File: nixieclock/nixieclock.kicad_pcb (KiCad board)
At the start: 2 copper layers, 21 parts, among them Q1 IRLR3110ZTRPBF, U1 LT3757AEMSE

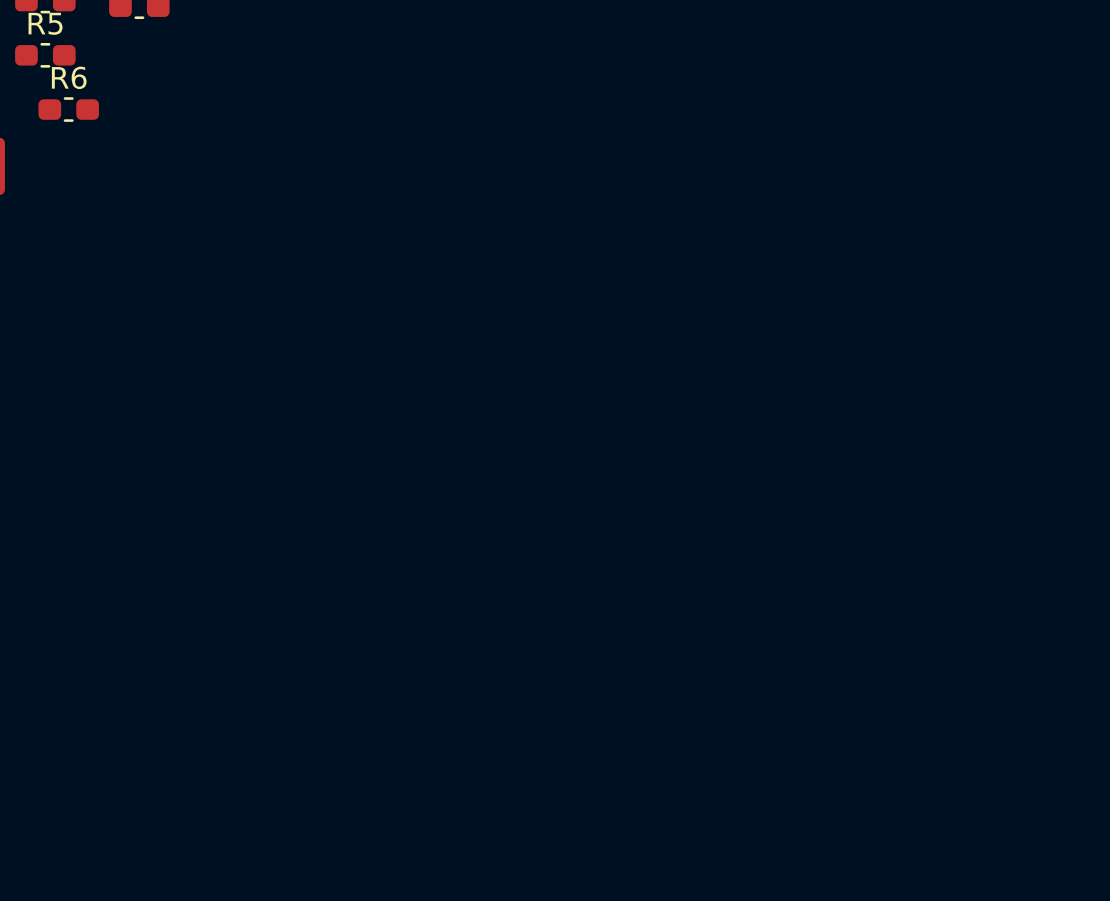
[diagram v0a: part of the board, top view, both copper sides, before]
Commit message: added nixie breakout, began shift registers
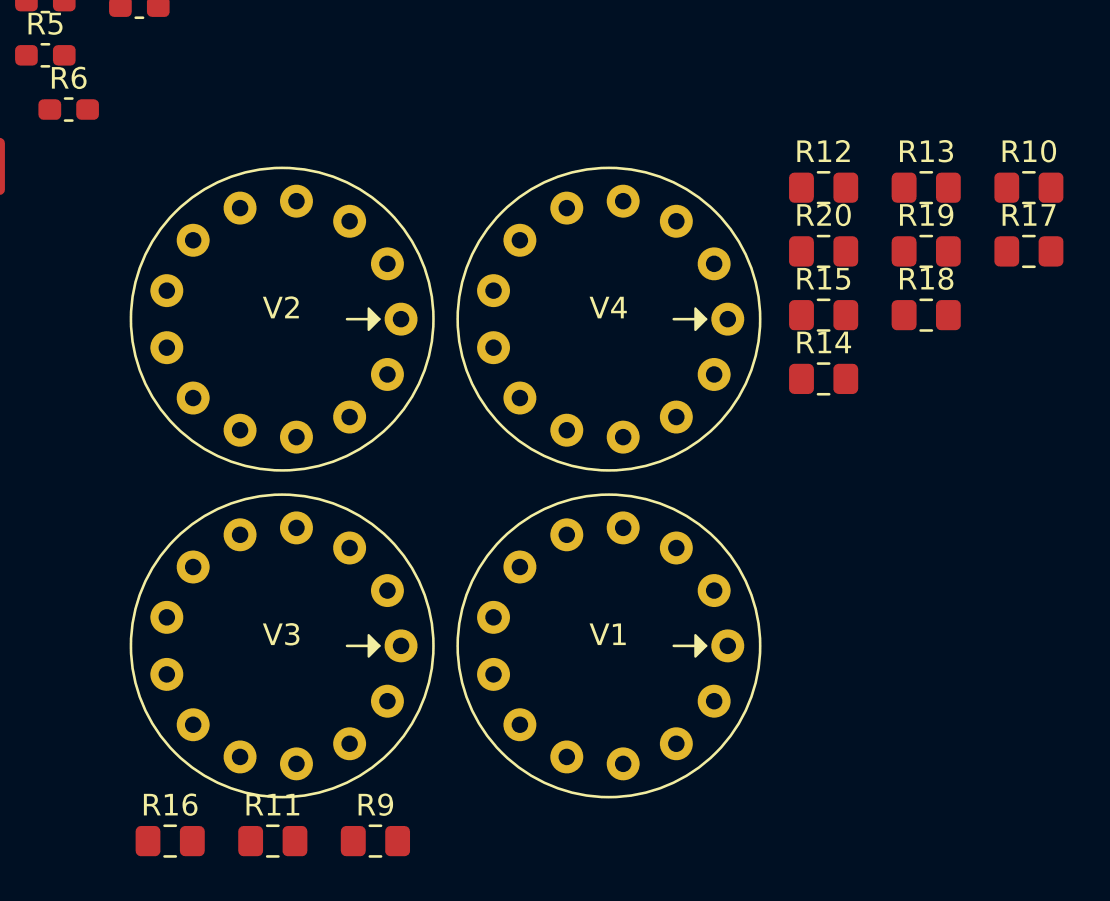
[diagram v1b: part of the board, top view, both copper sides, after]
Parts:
- added R10: R, Resistor_SMD:R_0805_2012Metric_Pad1.15x1.40mm_HandSolder, F.Cu at (261.4, 82.8)
- added R11: R, Resistor_SMD:R_0805_2012Metric_Pad1.15x1.40mm_HandSolder, F.Cu at (226.4, 113.0)
- added R12: R, Resistor_SMD:R_0805_2012Metric_Pad1.15x1.40mm_HandSolder, F.Cu at (251.9, 82.8)
- added R13: R, Resistor_SMD:R_0805_2012Metric_Pad1.15x1.40mm_HandSolder, F.Cu at (256.7, 82.8)
- added R14: R, Resistor_SMD:R_0805_2012Metric_Pad1.15x1.40mm_HandSolder, F.Cu at (251.9, 91.6)
- added R15: R, Resistor_SMD:R_0805_2012Metric_Pad1.15x1.40mm_HandSolder, F.Cu at (251.9, 88.7)
- added R16: R, Resistor_SMD:R_0805_2012Metric_Pad1.15x1.40mm_HandSolder, F.Cu at (221.7, 113.0)
- added R17: R, Resistor_SMD:R_0805_2012Metric_Pad1.15x1.40mm_HandSolder, F.Cu at (261.4, 85.7)
- added R18: R, Resistor_SMD:R_0805_2012Metric_Pad1.15x1.40mm_HandSolder, F.Cu at (256.7, 88.7)
- added R19: R, Resistor_SMD:R_0805_2012Metric_Pad1.15x1.40mm_HandSolder, F.Cu at (256.7, 85.7)
- added R20: R, Resistor_SMD:R_0805_2012Metric_Pad1.15x1.40mm_HandSolder, F.Cu at (251.9, 85.7)
- added R9: R, Resistor_SMD:R_0805_2012Metric_Pad1.15x1.40mm_HandSolder, F.Cu at (231.2, 113.0)
- added V1: IN14, Personal:IN-14, F.Cu at (242.0, 104.0)
- added V2: IN14, Personal:IN-14, F.Cu at (226.9, 88.9)
- added V3: IN14, Personal:IN-14, F.Cu at (226.9, 104.0)
- added V4: IN14, Personal:IN-14, F.Cu at (242.0, 88.9)

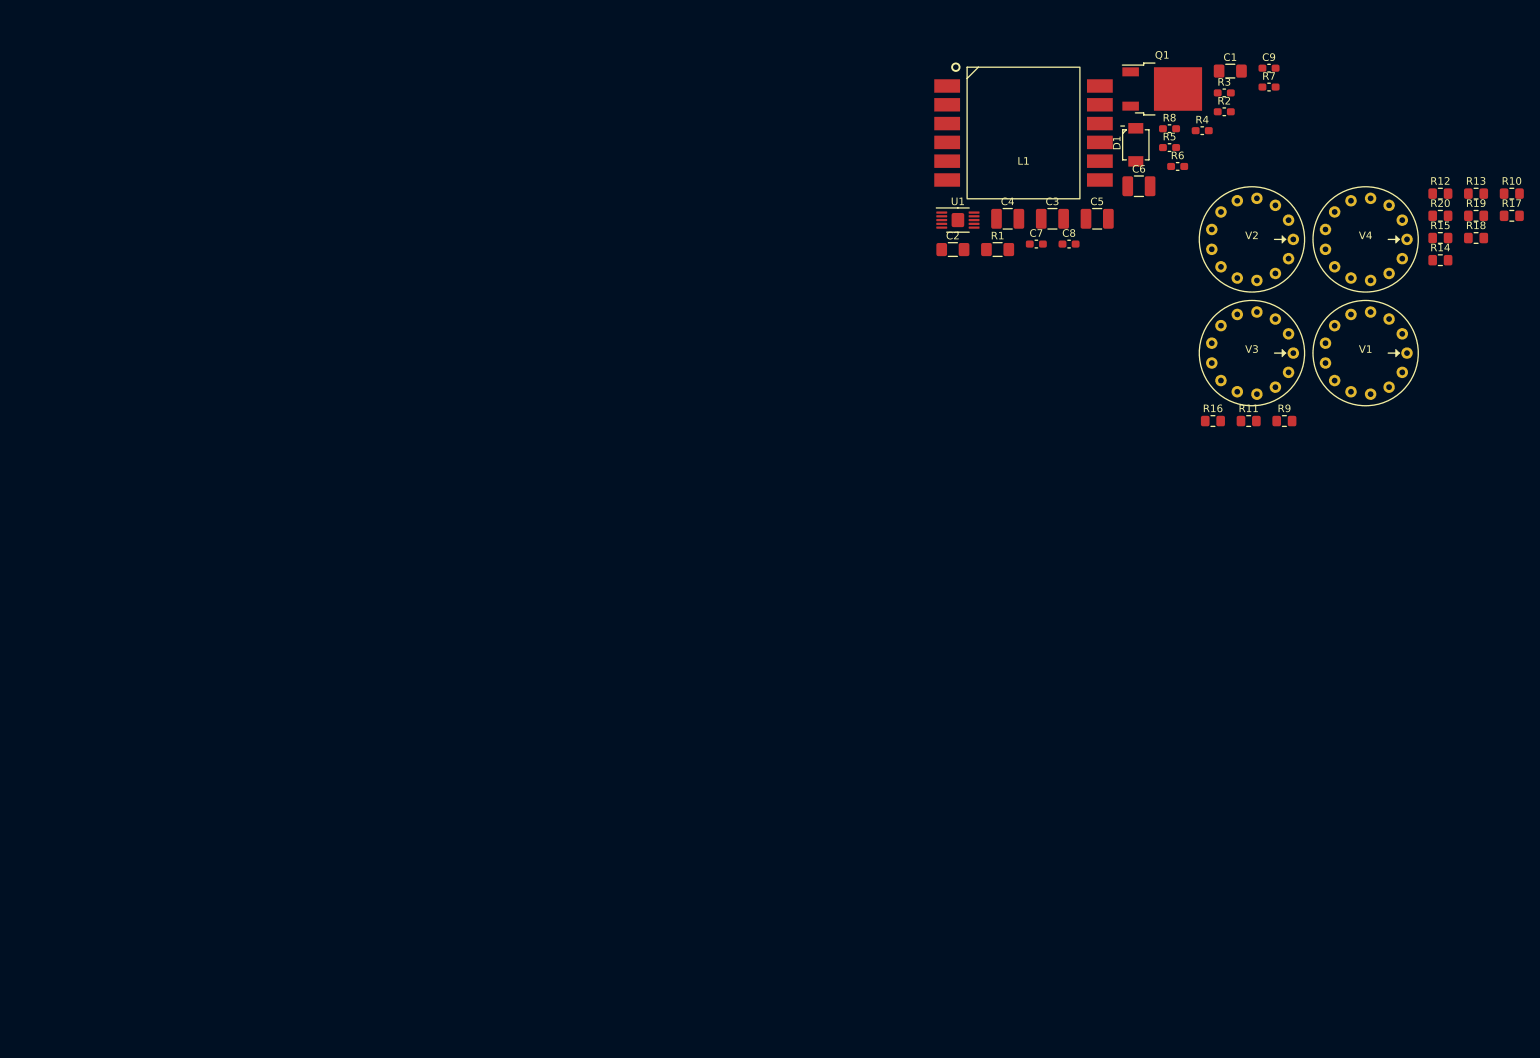
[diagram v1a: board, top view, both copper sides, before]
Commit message: finalized power supplies, most footprints, nixie breakout
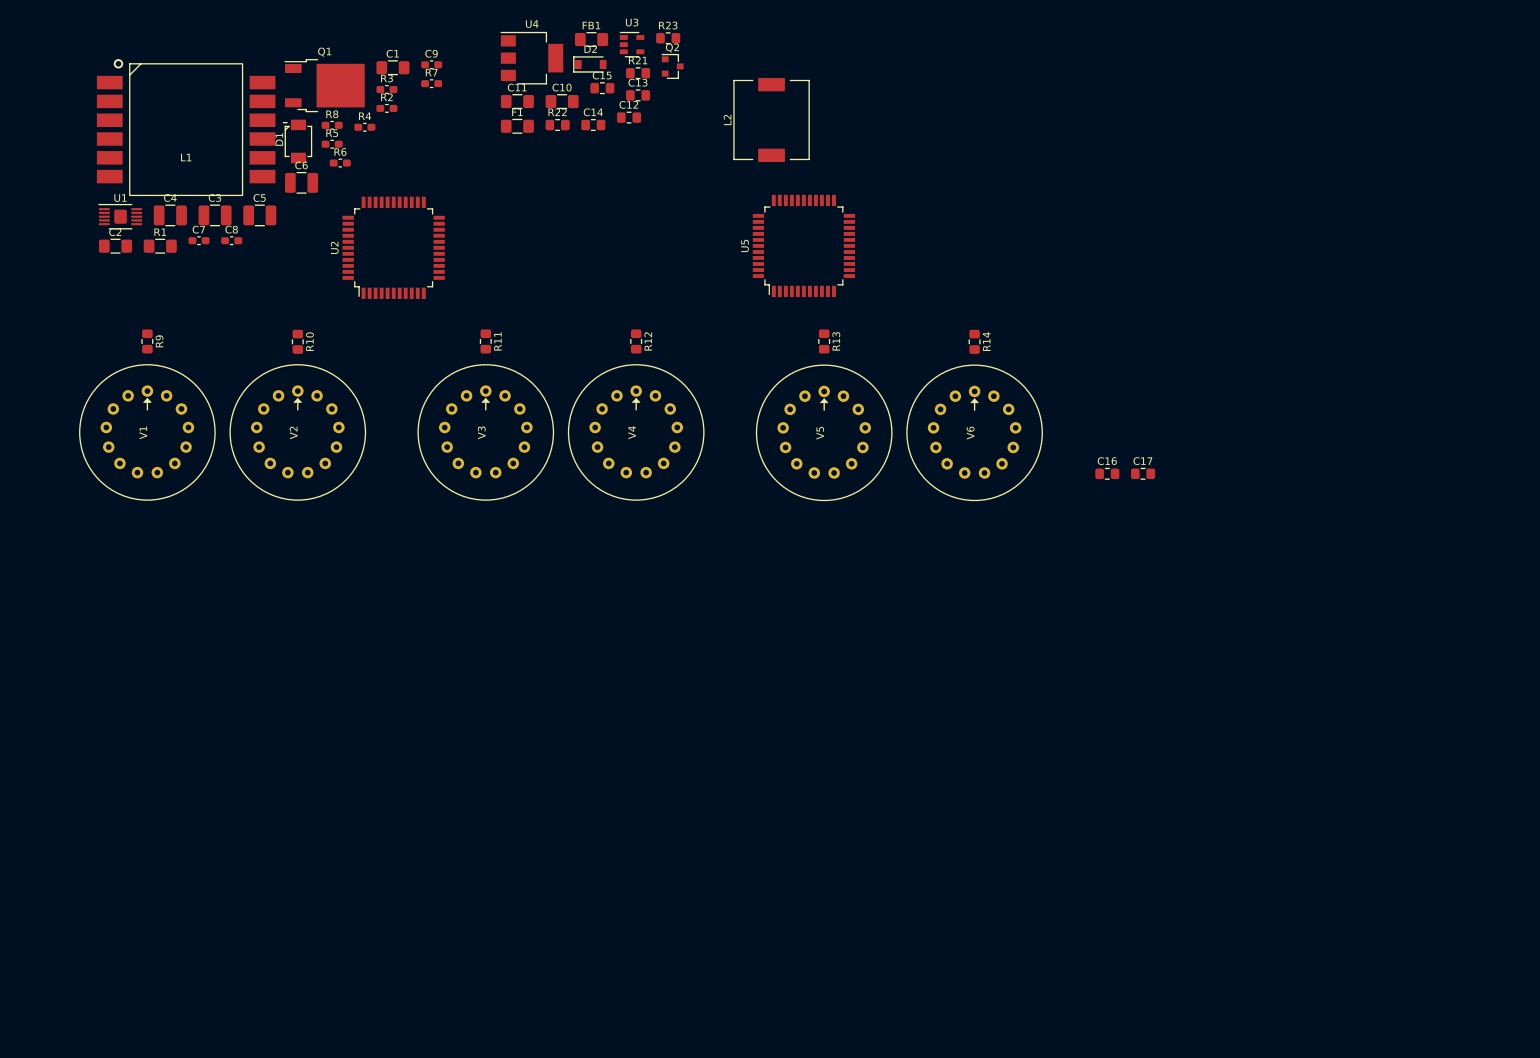
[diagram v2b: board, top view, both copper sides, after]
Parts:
- removed R15, R16, R17, R18, R19, R20: R, Resistor_SMD:R_0805_2012Metric_Pad1.15x1.40mm_HandSolder
- added C10: 10uF, Capacitor_SMD:C_1206_3216Metric_Pad1.42x1.75mm_HandSolder, F.Cu at (135.2, 70.5)
- added C11: 4.7uF, Capacitor_SMD:C_1206_3216Metric_Pad1.42x1.75mm_HandSolder, F.Cu at (129.2, 70.5)
- added C12: 2.2uF, Capacitor_SMD:C_0805_2012Metric_Pad1.15x1.40mm_HandSolder, F.Cu at (144.1, 72.7)
- added C13: 220pF, Capacitor_SMD:C_0805_2012Metric_Pad1.15x1.40mm_HandSolder, F.Cu at (145.2, 69.7)
- added C14: 10uF, Capacitor_SMD:C_0805_2012Metric_Pad1.15x1.40mm_HandSolder, F.Cu at (139.3, 73.7)
- added C15: 10uF, Capacitor_SMD:C_0805_2012Metric_Pad1.15x1.40mm_HandSolder, F.Cu at (140.5, 68.8)
- added C16: 100nF, Capacitor_SMD:C_0805_2012Metric_Pad1.15x1.40mm_HandSolder, F.Cu at (207.7, 120.0)
- added C17: 100nF, Capacitor_SMD:C_0805_2012Metric_Pad1.15x1.40mm_HandSolder, F.Cu at (212.4, 120.0)
- added D2: MBR0520, Diode_SMD:D_SOD-123, F.Cu at (138.9, 65.6)
- added F1: 1A, Fuse:Fuse_1206_3216Metric_Pad1.42x1.75mm_HandSolder, F.Cu at (129.2, 73.8)
- added FB1: 600 @ 600MHz, Inductor_SMD:L_1206_3216Metric_Pad1.42x1.75mm_HandSolder, F.Cu at (139.1, 62.3)
- added L2: 10uH, Personal:MSS1048-103MLB, F.Cu at (163.0, 73.0)
- added Q2: AO3401A, Package_TO_SOT_SMD:SOT-23, F.Cu at (149.8, 65.9)
- added R21: R, Resistor_SMD:R_0805_2012Metric_Pad1.15x1.40mm_HandSolder, F.Cu at (145.2, 66.8)
- added R22: 117k, Resistor_SMD:R_0805_2012Metric_Pad1.15x1.40mm_HandSolder, F.Cu at (134.6, 73.7)
- added R23: 13.3k, Resistor_SMD:R_0805_2012Metric_Pad1.15x1.40mm_HandSolder, F.Cu at (149.2, 62.1)
- added U2: HV5522, Package_QFP:PQFP-44_10x10mm_P0.8mm, F.Cu at (112.8, 90.0)
- added U3: LMR64010XMF, Package_TO_SOT_SMD:SOT-23-5, F.Cu at (144.4, 63.0)
- added U4: AMS1117-3.3, Package_TO_SOT_SMD:SOT-223-3_TabPin2, F.Cu at (131.2, 64.8)
- added U5: HV5522, Package_QFP:PQFP-44_10x10mm_P0.8mm, F.Cu at (167.3, 89.8)
- added V5: IN14, Personal:IN-14, F.Cu at (170.0, 114.6)
- added V6: IN14, Personal:IN-14, F.Cu at (190.0, 114.6)
- moved R10 162.6 mm to (100.0, 102.5), turned to -90 degrees
- moved V1 162.3 mm to (80.0, 114.5), turned to 90 degrees
- moved R9 151.6 mm to (80.0, 102.5), turned to -90 degrees
- moved V2 129.5 mm to (100.0, 114.5), turned to 90 degrees
- moved C2 111.4 mm to (75.8, 89.8)
- moved C4 111.4 mm to (83.0, 85.7)
- moved C5 111.4 mm to (95.0, 85.7)
- moved C7 111.4 mm to (86.9, 89.0)
- moved C8 111.4 mm to (91.2, 89.0)
- moved C9 111.4 mm to (117.8, 65.7)
- moved D1 111.4 mm to (100.1, 75.9)
- moved R1 111.4 mm to (81.7, 89.8)
- moved R4 111.4 mm to (108.9, 74.0)
- moved R7 111.4 mm to (117.8, 68.2)
- moved C1 111.4 mm to (112.7, 66.0)
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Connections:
- net /hv_supply/FBX renamed /power_supply/FBX
- R13 pad 1: (no net) -> HV
- R14 pad 1: (no net) -> HV
- V1 pad 10: (no net) -> /NA8
- V1 pad 11: (no net) -> /NA9
- V1 pad 12: (no net) -> /NA0
- V1 pad 13: Net-(R17-Pad1) -> (no net)
- V1 pad 2: Net-(R13-Pad2) -> (no net)
- V1 pad 3: (no net) -> /NA1
- V1 pad 4: (no net) -> /NA2
- V1 pad 5: (no net) -> /NA3
- V1 pad 6: (no net) -> /NA4
- V1 pad 7: (no net) -> /NA5
- V1 pad 8: (no net) -> /NA6
- V1 pad 9: (no net) -> /NA7
- V2 pad 10: (no net) -> /NB8
- V2 pad 11: (no net) -> /NB9
- V2 pad 12: (no net) -> /NB0
- V2 pad 13: Net-(R18-Pad1) -> (no net)
- V2 pad 2: Net-(R14-Pad2) -> (no net)
- V2 pad 3: (no net) -> /NB1
- V2 pad 4: (no net) -> /NB2
- V2 pad 5: (no net) -> /NB3
- V2 pad 6: (no net) -> /NB4
- V2 pad 7: (no net) -> /NB5
- V2 pad 8: (no net) -> /NB6
- V2 pad 9: (no net) -> /NB7
- V3 pad 10: (no net) -> /NC8
- V3 pad 11: (no net) -> /NC9
- V3 pad 12: (no net) -> /NC0
- V3 pad 13: Net-(R19-Pad1) -> (no net)
- V3 pad 2: Net-(R15-Pad2) -> (no net)
- V3 pad 3: (no net) -> /NC1
- V3 pad 4: (no net) -> /NC2
- V3 pad 5: (no net) -> /NC3
- V3 pad 6: (no net) -> /NC4
- V3 pad 7: (no net) -> /NC5
- V3 pad 8: (no net) -> /NC6
- V3 pad 9: (no net) -> /NC7
- V4 pad 10: (no net) -> /ND8
- V4 pad 11: (no net) -> /ND9
- V4 pad 12: (no net) -> /ND0
- V4 pad 13: Net-(R20-Pad1) -> (no net)
- V4 pad 2: Net-(R16-Pad2) -> (no net)
- V4 pad 3: (no net) -> /ND1
- V4 pad 4: (no net) -> /ND2
- V4 pad 5: (no net) -> /ND3
- V4 pad 6: (no net) -> /ND4
- V4 pad 7: (no net) -> /ND5
- V4 pad 8: (no net) -> /ND6
- V4 pad 9: (no net) -> /ND7

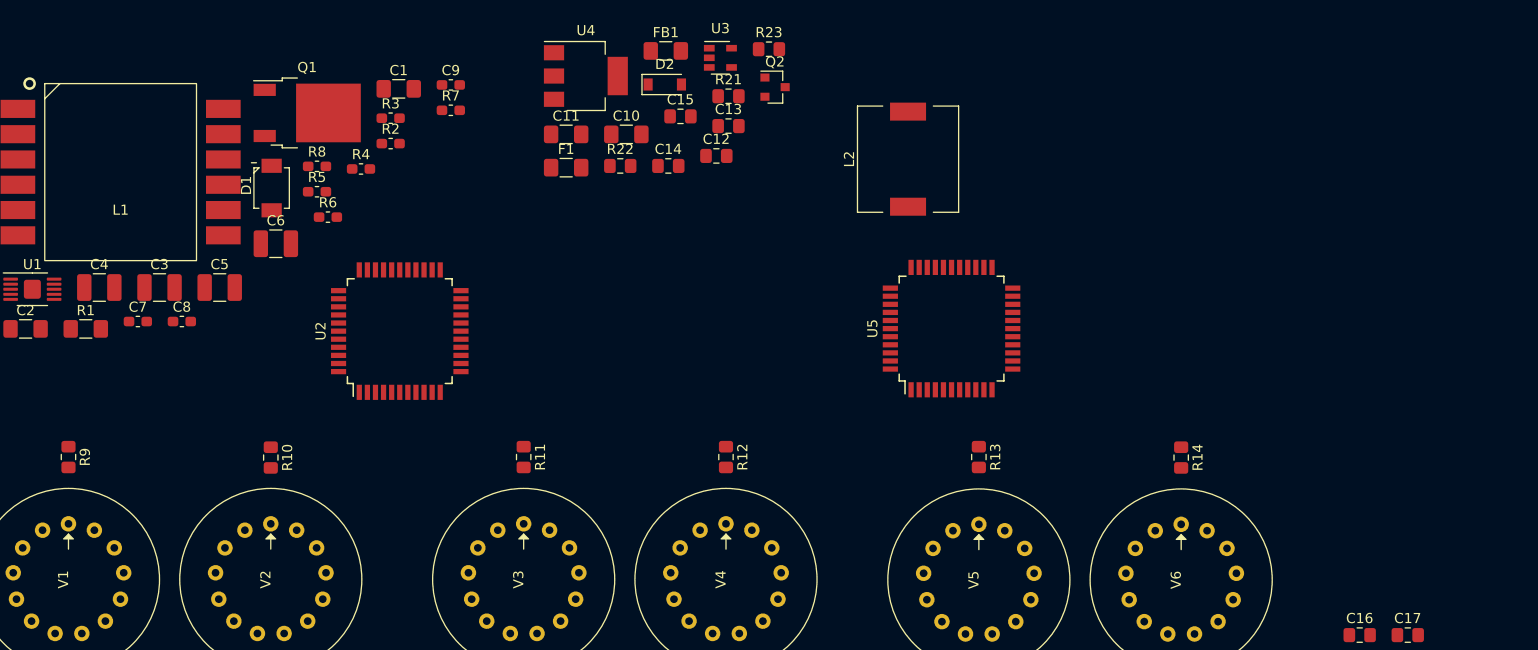
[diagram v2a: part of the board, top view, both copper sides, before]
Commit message: added neon bulbs, finalized cathode registers
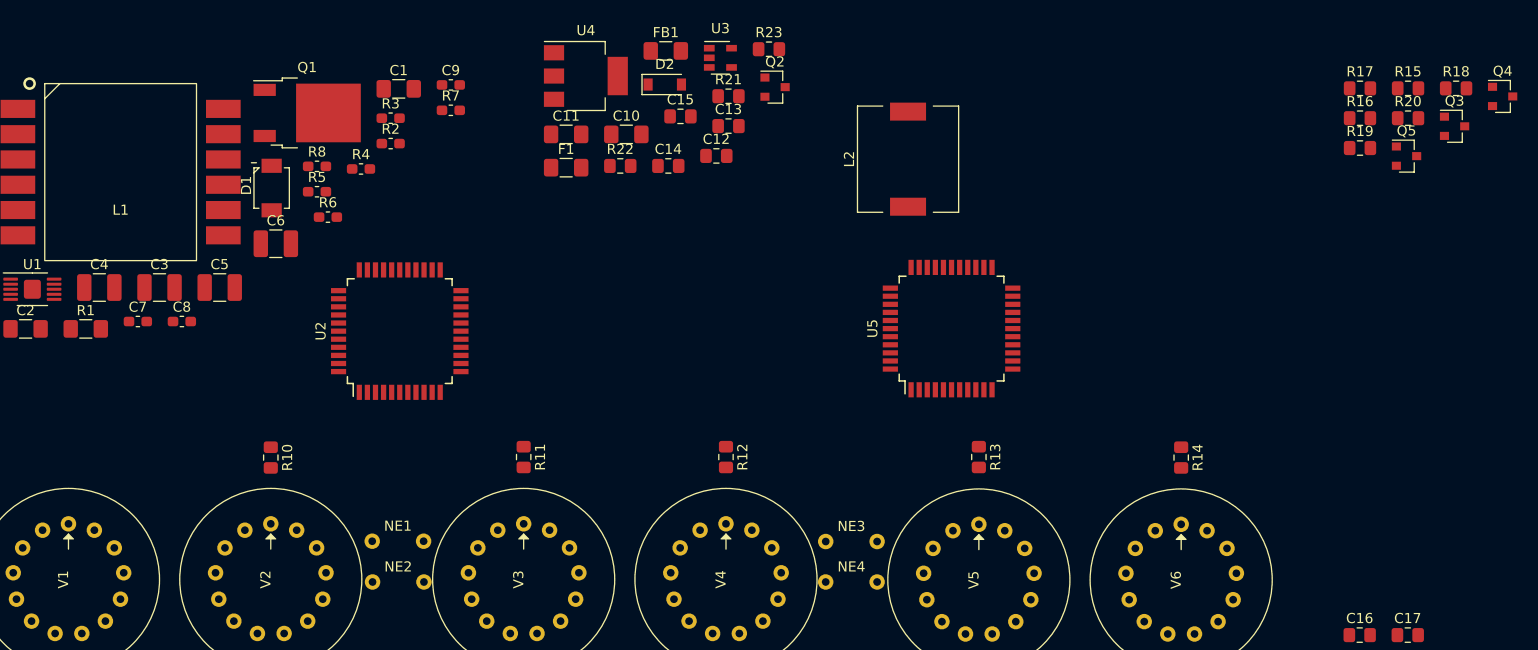
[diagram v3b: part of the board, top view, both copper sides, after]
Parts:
- removed R9: R, Resistor_SMD:R_0805_2012Metric_Pad1.15x1.40mm_HandSolder
- added NE1: NE-2, Personal:NE-2, F.Cu at (112.6, 110.8)
- added NE2: NE-2, Personal:NE-2, F.Cu at (112.6, 114.8)
- added NE3: NE-2, Personal:NE-2, F.Cu at (157.4, 110.8)
- added NE4: NE-2, Personal:NE-2, F.Cu at (157.4, 114.8)
- added Q3: BSS138, Package_TO_SOT_SMD:SOT-23, F.Cu at (217.0, 69.8)
- added Q4: BSS138, Package_TO_SOT_SMD:SOT-23, F.Cu at (221.8, 66.8)
- added Q5: BSS138, Package_TO_SOT_SMD:SOT-23, F.Cu at (212.3, 72.7)
- added R15: 2.21k, Resistor_SMD:R_0805_2012Metric_Pad1.15x1.40mm_HandSolder, F.Cu at (212.4, 66.0)
- added R16: 2.21k, Resistor_SMD:R_0805_2012Metric_Pad1.15x1.40mm_HandSolder, F.Cu at (207.7, 69.0)
- added R17: 2.21k, Resistor_SMD:R_0805_2012Metric_Pad1.15x1.40mm_HandSolder, F.Cu at (207.7, 66.0)
- added R18: 2.21k, Resistor_SMD:R_0805_2012Metric_Pad1.15x1.40mm_HandSolder, F.Cu at (217.2, 66.0)
- added R19: 2.21k, Resistor_SMD:R_0805_2012Metric_Pad1.15x1.40mm_HandSolder, F.Cu at (207.7, 71.9)
- added R20: 2.21k, Resistor_SMD:R_0805_2012Metric_Pad1.15x1.40mm_HandSolder, F.Cu at (212.4, 69.0)
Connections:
- C1 pad 1: Net-(C1-Pad1) -> HV
- C2 pad 1: Net-(C1-Pad1) -> HV
- D1 pad 1: Net-(C1-Pad1) -> HV
- R1 pad 1: Net-(C1-Pad1) -> HV
- U2 pad 27: (no net) -> +12V
- U2 pad 28: (no net) -> /cathode_registers/HV_CLK
- U2 pad 31: (no net) -> /cathode_registers/~HV_LE
- U2 pad 32: (no net) -> /cathode_registers/HV_DIN
- U2 pad 33: (no net) -> +12V
- U5 pad 27: (no net) -> +12V
- U5 pad 28: (no net) -> /cathode_registers/HV_CLK
- U5 pad 31: (no net) -> /cathode_registers/~HV_LE
- U5 pad 33: (no net) -> +12V
- V1 pad 1: Net-(R9-Pad2) -> (no net)
